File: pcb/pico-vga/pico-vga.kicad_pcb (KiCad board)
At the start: 2 copper layers, 60.4 x 83.3 mm, 47 parts, among them J1 DB15_Female_HighDensity, J2 Micro_SD_Card_Det, J3 USB_A, J4 USB_A, J5 Conn_01x04_Male, J6 AudioJack3, J7 Conn_01x02_Male, J8 USB_A, J9 USB_A, Q1 DMP3099L-7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

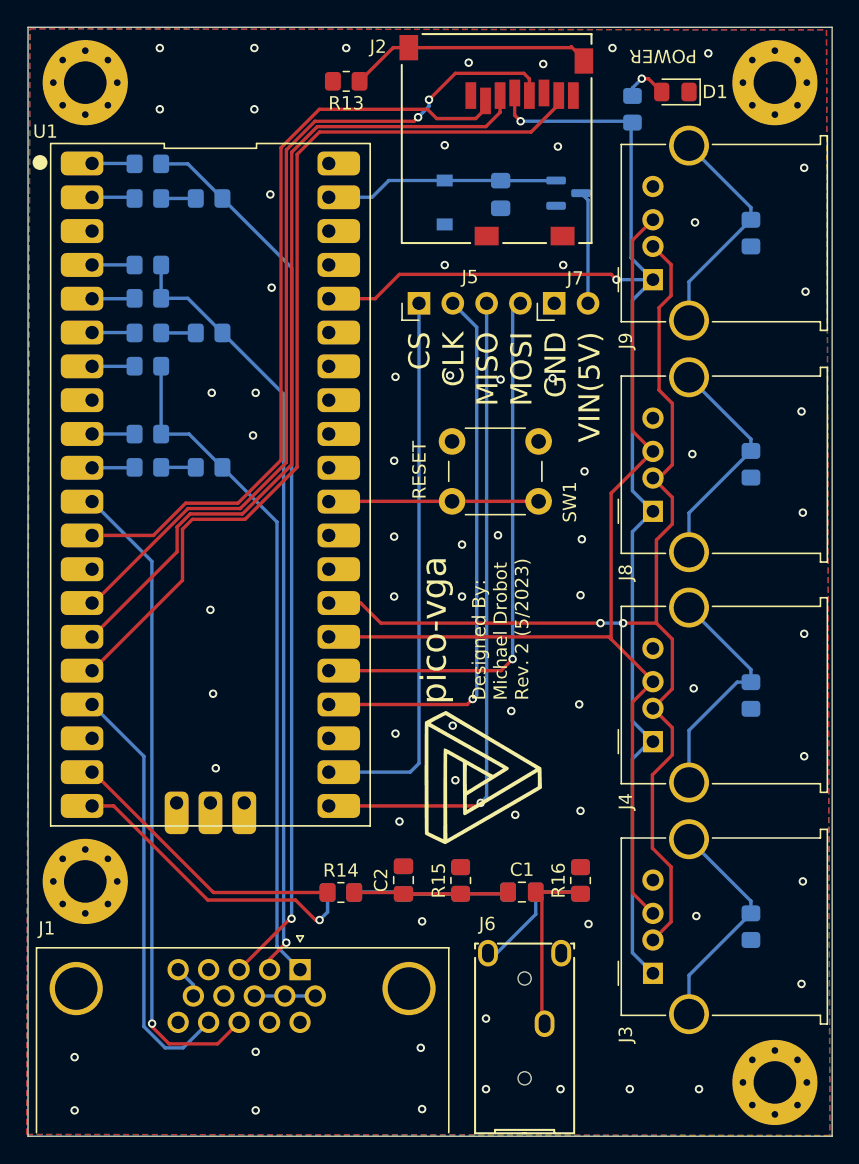
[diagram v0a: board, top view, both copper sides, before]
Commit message: Forgot I2C pullup resistors, updated Sch, PCB, and BOM
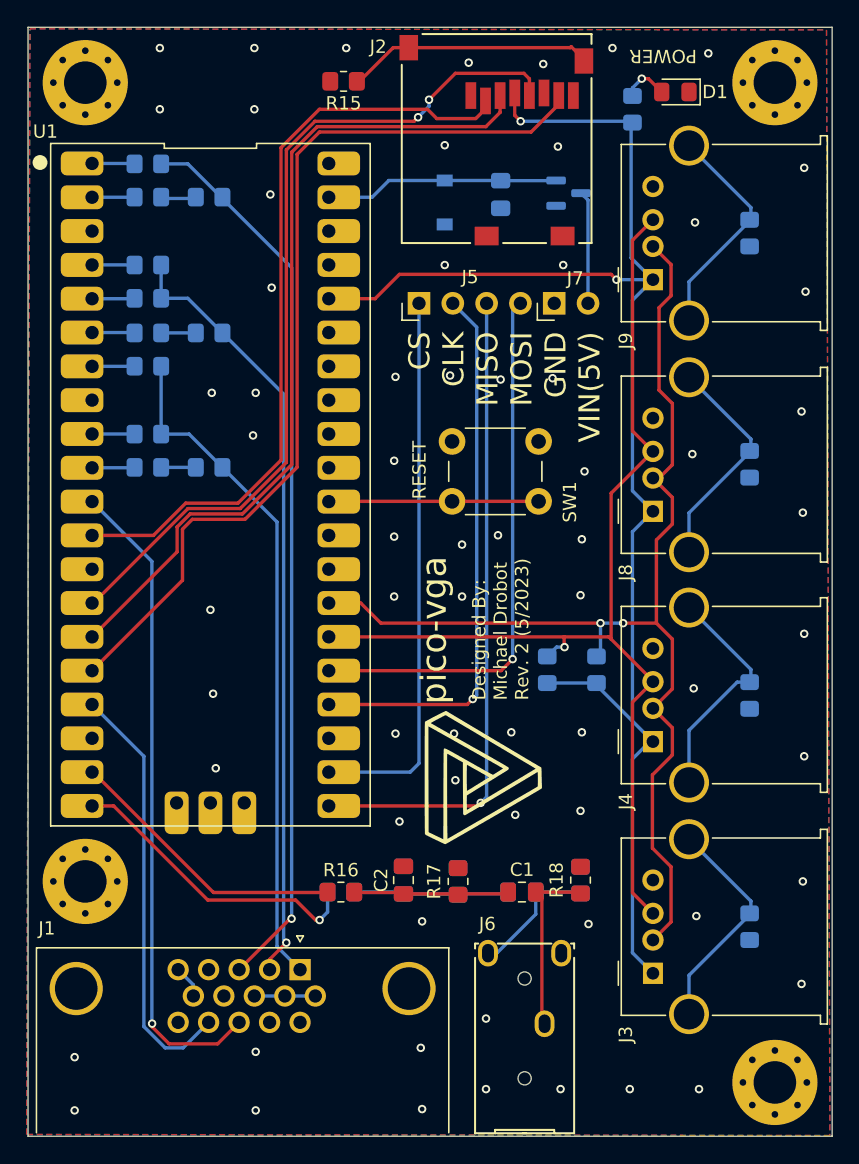
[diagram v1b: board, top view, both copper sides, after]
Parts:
- added R24: 1M, Resistor_SMD:R_0805_2012Metric_Pad1.20x1.40mm_HandSolder, B.Cu at (68.8, 45.3)
- added R25: 1M, Resistor_SMD:R_0805_2012Metric_Pad1.20x1.40mm_HandSolder, B.Cu at (68.8, 27.9)
- R10: value 390 -> 4.7k
- R11: value 47 -> 4.7k
- R12: value 1K -> 390
- R13: value 1M -> 47; moved to B.Cu
- R14: value 220 -> 1K; moved to B.Cu
- R15, R20: value 100 -> 1M
- R16, R21: value 1.8K -> 220
- R17: value 1M -> 100; moved to F.Cu
- R18: value 1M -> 1.8K; moved to F.Cu
- R19: value 220 -> 1M
- R22: value 1M -> 100
- R23: value 1M -> 1.8K
- moved R15 60.7 mm to (38.3, 16.5), turned to 180 degrees
- moved R14 56.6 mm to (23.6, 22.7)
- moved R23 50.3 mm to (56.1, 76.5)
- moved R10 48.9 mm to (57.3, 60.7), turned to -90 degrees
- moved R11 43.6 mm to (53.6, 60.7), turned to -90 degrees
- moved R22 38.3 mm to (46.9, 76.6)
- moved R19 30.8 mm to (68.8, 80.0), turned to 90 degrees
- moved R20 25.8 mm to (68.8, 62.6)
- moved R17 22.3 mm to (46.9, 76.6)
- moved R18 18.9 mm to (56.1, 76.5)
- moved R16 18.0 mm to (38.1, 77.4), turned to 0 degrees
- moved R21 18.0 mm to (38.1, 77.4), turned to 0 degrees
- moved R13 13.5 mm to (28.2, 25.2), turned to 0 degrees
- moved R12 2.50 mm to (23.6, 25.2)
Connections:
- J2 pad 11: Net-(R13-Pad1) -> Net-(J2-Pad11)
- R10 pad 1: /BLUE_1 -> /CONTROLLER_SCL
- R10 pad 2: Net-(R10-Pad2) -> +3V3
- R11 pad 1: Net-(R10-Pad2) -> /CONTROLLER_SDA
- R11 pad 2: Net-(J1-Pad3) -> +3V3
- R12 pad 1: /BLUE_2 -> /BLUE_1
- R12 pad 2: Net-(J1-Pad3) -> Net-(R12-Pad2)
- R13 pad 1: Net-(R13-Pad1) -> Net-(R12-Pad2)
- R13 pad 2: GND -> Net-(J1-Pad3)
- R14 pad 1: /AUDIO_L -> /BLUE_2
- R14 pad 2: Net-(C1-Pad1) -> Net-(J1-Pad3)
- R15 pad 1: Net-(C1-Pad1) -> Net-(J2-Pad11)
- R16 pad 1: Net-(C1-Pad2) -> /AUDIO_L
- R16 pad 2: GND -> Net-(C1-Pad1)
- R17 pad 1: GND -> Net-(C1-Pad1)
- R17 pad 2: Net-(J3-Pad5) -> GND
- R18 pad 1: GND -> Net-(C1-Pad2)
- R18 pad 2: Net-(J4-Pad5) -> GND
- R19 pad 1: /AUDIO_R -> GND
- R19 pad 2: Net-(C3-Pad1) -> Net-(J3-Pad5)
- R20 pad 1: Net-(C3-Pad1) -> GND
- R20 pad 2: GND -> Net-(J4-Pad5)
- R21 pad 1: Net-(C3-Pad2) -> /AUDIO_R
- R21 pad 2: GND -> Net-(C3-Pad1)
- R22 pad 1: GND -> Net-(C3-Pad1)
- R22 pad 2: Net-(J8-Pad5) -> GND
- R23 pad 1: GND -> Net-(C3-Pad2)
- R23 pad 2: Net-(J9-Pad5) -> GND
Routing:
- net Net-(R13-Pad1): track 18.3 -> 0.00 mm
- net Net-(J2-Pad11): track 0.00 -> 18.3 mm
- net +3V3: track 104.1 -> 111.8 mm
- net /CONTROLLER_SCL: track 83.7 -> 86.3 mm
- net Net-(R12-Pad2): track 0.00 -> 2.60 mm
- net Net-(R10-Pad2): track 2.60 -> 0.00 mm
- net /CONTROLLER_SDA: track 78.5 -> 80.8 mm, vias 0 -> 1

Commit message: Revert "Forgot I2C pullup resistors, updated Sch, PCB, and BOM"
Don't need the pullups, you can do it internally in software. No point adding them and making the BOM longer.

This reverts commit bd8d0dffae4885964e3fb42256447820ac871936.
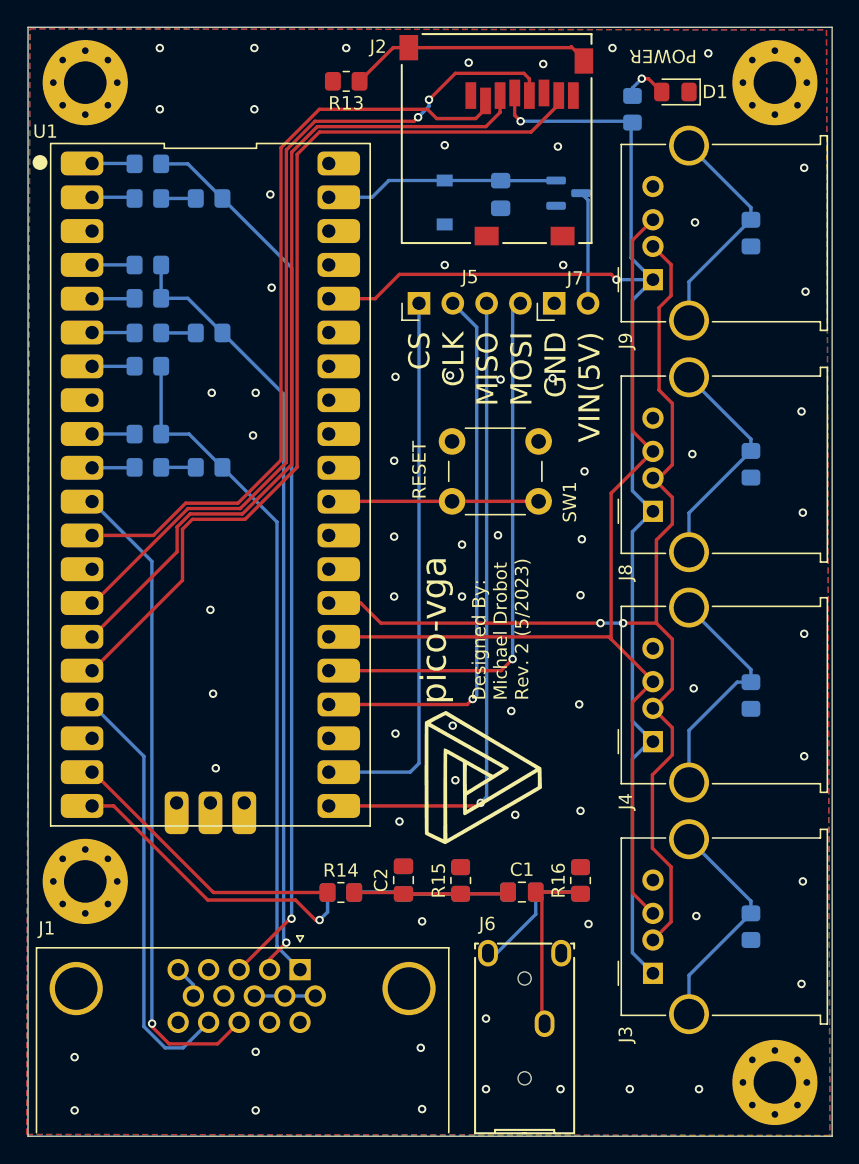
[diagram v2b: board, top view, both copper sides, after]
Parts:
- removed R24, R25: 1M, Resistor_SMD:R_0805_2012Metric_Pad1.20x1.40mm_HandSolder
- R10: value 4.7k -> 390
- R11: value 4.7k -> 47
- R12: value 390 -> 1K
- R13: value 47 -> 1M; moved to F.Cu
- R14: value 1K -> 220; moved to F.Cu
- R15, R20: value 1M -> 100
- R16, R21: value 220 -> 1.8K
- R17: value 100 -> 1M; moved to B.Cu
- R18: value 1.8K -> 1M; moved to B.Cu
- R19: value 1M -> 220
- R22: value 100 -> 1M
- R23: value 1.8K -> 1M
- moved R15 60.7 mm to (47.1, 76.5), turned to 90 degrees
- moved R14 56.6 mm to (38.1, 77.4)
- moved R23 50.3 mm to (68.9, 27.9)
- moved R10 48.9 mm to (23.6, 25.3), turned to 0 degrees
- moved R11 43.6 mm to (28.2, 25.3), turned to 0 degrees
- moved R22 38.3 mm to (68.9, 45.3)
- moved R19 30.8 mm to (38.1, 77.4), turned to 0 degrees
- moved R20 25.8 mm to (47.1, 76.5)
- moved R17 22.3 mm to (68.9, 80.0)
- moved R18 18.9 mm to (68.9, 62.6)
- moved R16 18.0 mm to (56.1, 76.5), turned to 90 degrees
- moved R21 18.0 mm to (56.1, 76.5), turned to 90 degrees
- moved R13 13.5 mm to (38.5, 16.5), turned to 180 degrees
- moved R12 2.50 mm to (23.6, 22.7)
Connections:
- J2 pad 11: Net-(J2-Pad11) -> Net-(R13-Pad1)
- R10 pad 1: /CONTROLLER_SCL -> /BLUE_1
- R10 pad 2: +3V3 -> Net-(R10-Pad2)
- R11 pad 1: /CONTROLLER_SDA -> Net-(R10-Pad2)
- R11 pad 2: +3V3 -> Net-(J1-Pad3)
- R12 pad 1: /BLUE_1 -> /BLUE_2
- R12 pad 2: Net-(R12-Pad2) -> Net-(J1-Pad3)
- R13 pad 1: Net-(R12-Pad2) -> Net-(R13-Pad1)
- R13 pad 2: Net-(J1-Pad3) -> GND
- R14 pad 1: /BLUE_2 -> /AUDIO_L
- R14 pad 2: Net-(J1-Pad3) -> Net-(C1-Pad1)
- R15 pad 1: Net-(J2-Pad11) -> Net-(C1-Pad1)
- R16 pad 1: /AUDIO_L -> Net-(C1-Pad2)
- R16 pad 2: Net-(C1-Pad1) -> GND
- R17 pad 1: Net-(C1-Pad1) -> GND
- R17 pad 2: GND -> Net-(J3-Pad5)
- R18 pad 1: Net-(C1-Pad2) -> GND
- R18 pad 2: GND -> Net-(J4-Pad5)
- R19 pad 1: GND -> /AUDIO_R
- R19 pad 2: Net-(J3-Pad5) -> Net-(C3-Pad1)
- R20 pad 1: GND -> Net-(C3-Pad1)
- R20 pad 2: Net-(J4-Pad5) -> GND
- R21 pad 1: /AUDIO_R -> Net-(C3-Pad2)
- R21 pad 2: Net-(C3-Pad1) -> GND
- R22 pad 1: Net-(C3-Pad1) -> GND
- R22 pad 2: GND -> Net-(J8-Pad5)
- R23 pad 1: Net-(C3-Pad2) -> GND
- R23 pad 2: GND -> Net-(J9-Pad5)
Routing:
- net Net-(R13-Pad1): track 0.00 -> 18.3 mm
- net Net-(J2-Pad11): track 18.3 -> 0.00 mm
- net +3V3: track 111.8 -> 104.1 mm
- net /CONTROLLER_SCL: track 86.3 -> 83.7 mm
- net Net-(R12-Pad2): track 2.60 -> 0.00 mm
- net Net-(R10-Pad2): track 0.00 -> 2.60 mm
- net /CONTROLLER_SDA: track 80.8 -> 78.5 mm, vias 1 -> 0
